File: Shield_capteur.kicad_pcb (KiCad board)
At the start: 2 copper layers, 79.2 x 66.2 mm, 23 parts, among them J1 Power, J2 Digital/PWM, J3 Analog, J4 Digital/PWM, K63 1uF, U1 LTC1050ACN8_PBF, U2 MCP

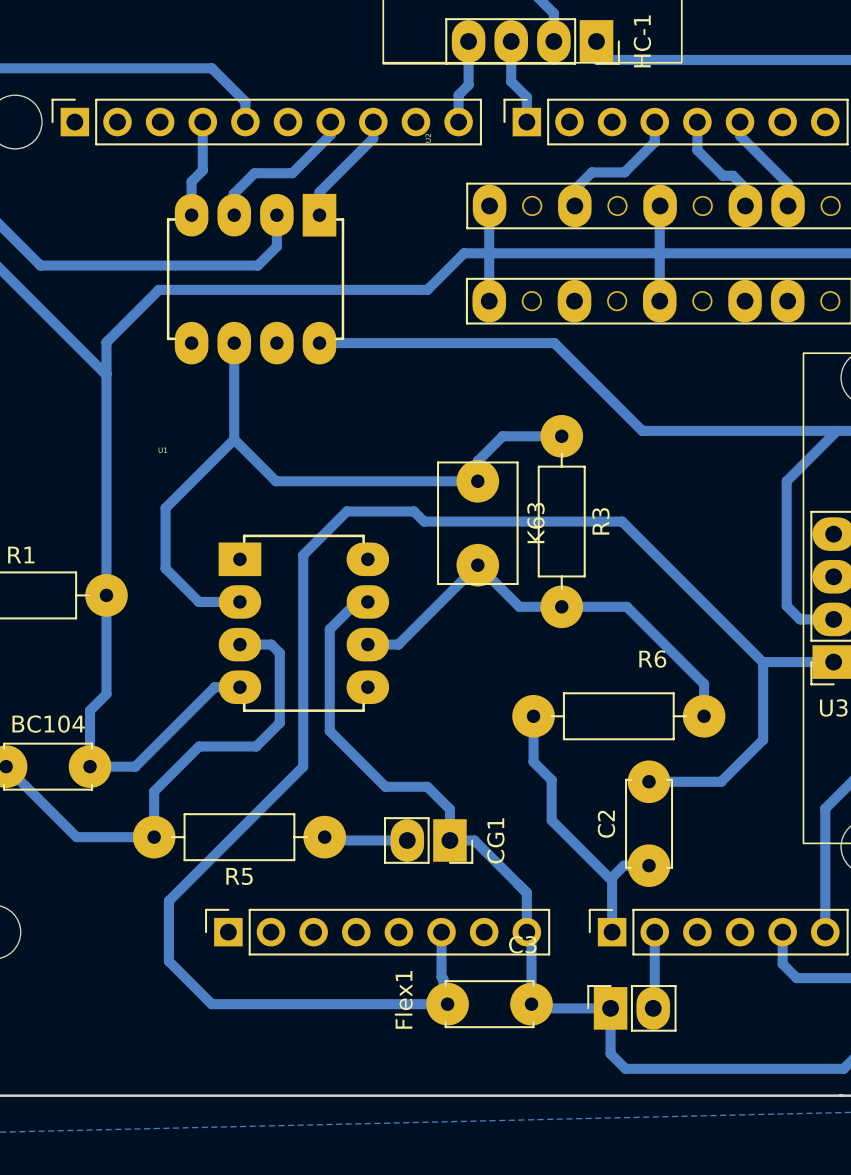
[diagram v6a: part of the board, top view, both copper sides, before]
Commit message: Correction du PCB il reste connection RFlex
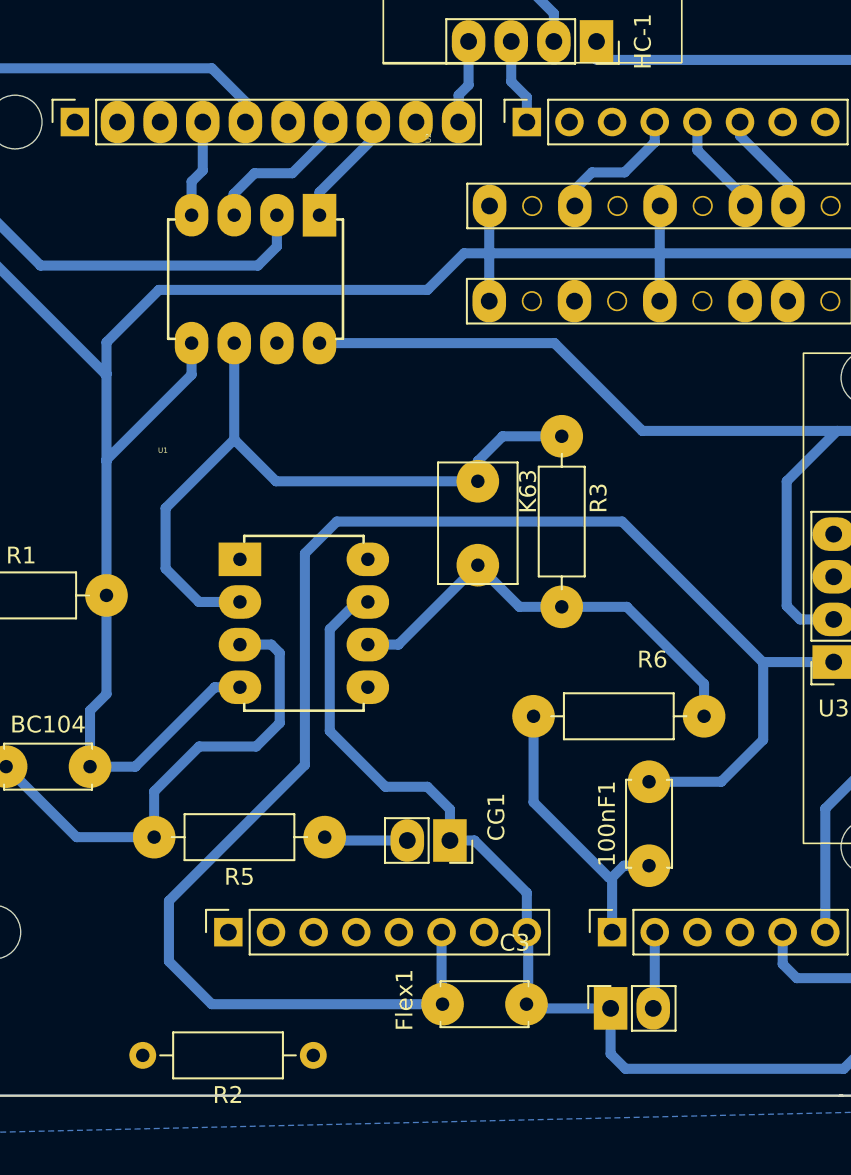
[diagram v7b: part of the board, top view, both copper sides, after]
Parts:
- added R2: R, Resistor_THT:R_Axial_DIN0207_L6.3mm_D2.5mm_P10.16mm_Horizontal, F.Cu at (133.0, 104.8)
- moved C3 0.30 mm to (140.7, 101.8)
- renumbered C2 to 100nF1
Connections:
- U2 pad 5: unconnected-(U2-PA0-Pad5) -> GND
- U2 pad 6: Net-(U1--IN) -> GND
- U2 pad 7: unconnected-(U2-PB0-Pad7) -> Net-(U1--IN)
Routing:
- net GND: track 272.9 -> 282.1 mm

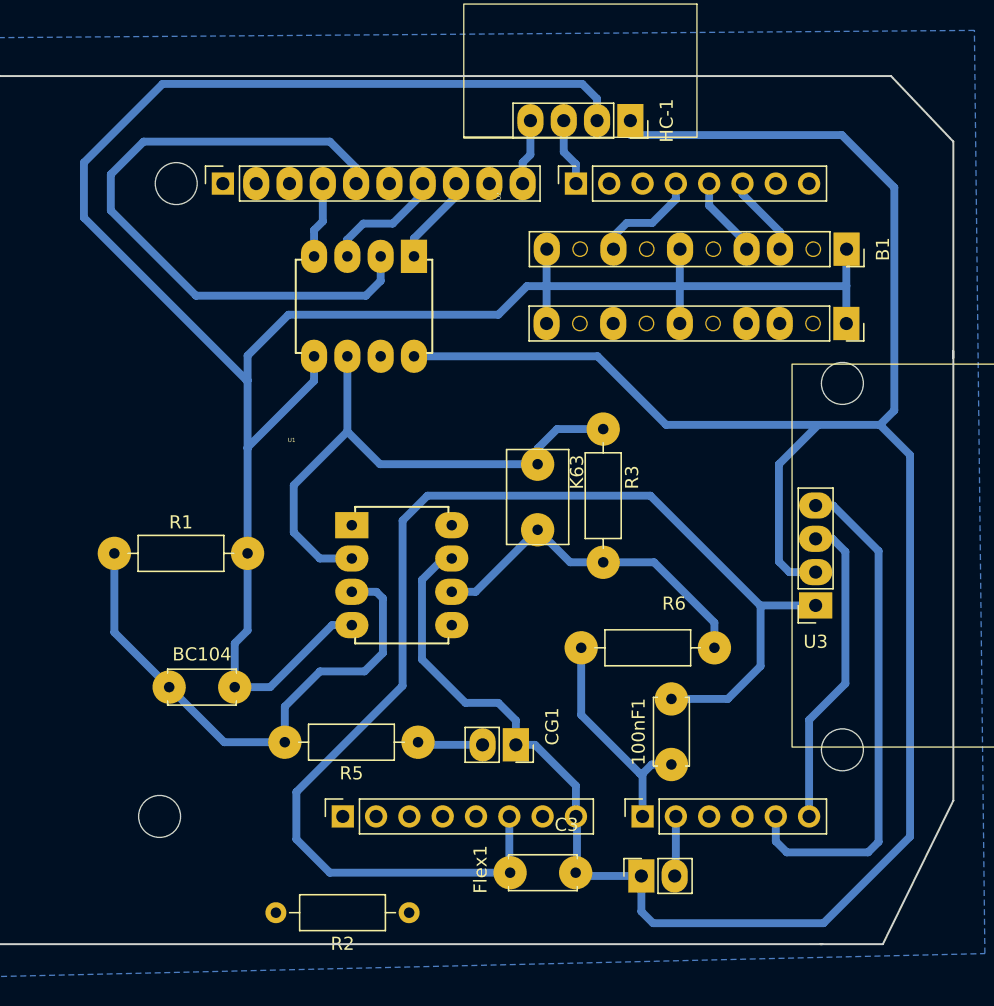
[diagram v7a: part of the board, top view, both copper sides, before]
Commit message: Changement de la largeur des pistes de 0.6mm à 0.8mm
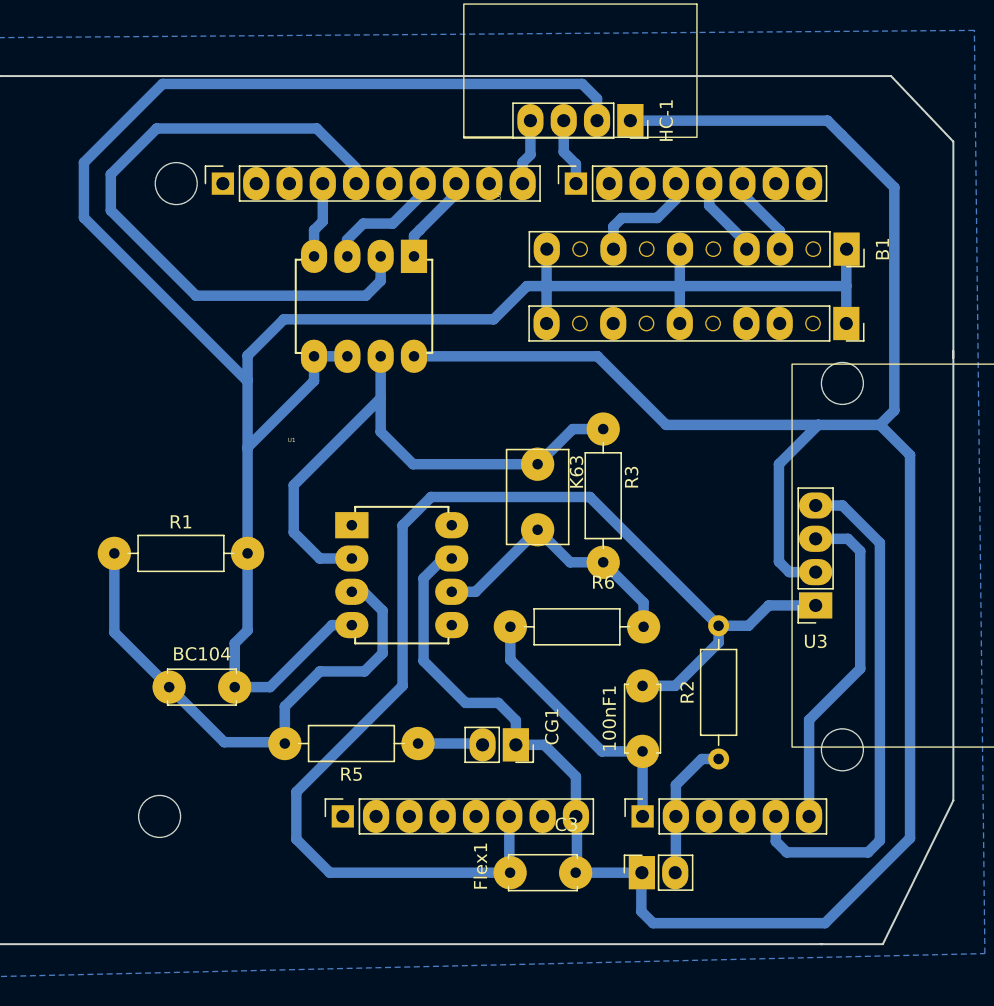
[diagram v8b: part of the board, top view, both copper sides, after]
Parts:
- moved R2 26.3 mm to (156.6, 93.1), turned to 90 degrees
- moved R6 5.63 mm to (140.7, 83.0)
- moved 100nF1 2.42 mm to (150.8, 92.5)
- moved Flex1 0.25 mm to (150.8, 101.8)
- moved R5 0.10 mm to (133.7, 91.9)
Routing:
- net /A1: track 4.58 -> 11.0 mm
- net Net-(U1-OUT): track 26.8 -> 20.7 mm
- net /A0: track 17.4 -> 20.5 mm
- net /SCL: track 24.0 -> 25.6 mm
- net GND: track 282.1 -> 280.5 mm
- net VCC: track 189.8 -> 191.2 mm
- net /D13: track 50.1 -> 51.0 mm
- net /D2: track 6.18 -> 7.00 mm
- net Net-(U1-+IN): track 41.1 -> 40.5 mm
- net /SDA: track 38.8 -> 39.3 mm
